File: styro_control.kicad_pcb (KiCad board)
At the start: 4 copper layers, 100.3 x 54 mm, 125 parts, among them J3 INPUT_PEDAL, J4 SWD, Q1 IRF7324, Q2 Q_NPN_BEC, Q3 Q_NMOS_GDS, Q4 Q_NPN_BEC, Q5 Q_NMOS_GDS, Q6 Q_NPN_BEC, Q7 Q_NMOS_GDS, Q8 Q_NPN_BEC, Q9 Q_NMOS_GDS, SW1 SW_RESET, SW2 switch_6_pin, SW3 SW_1, SW4 SW_2, SW5 SW_3, U1 STUSB4500QTR, U2 PAC1932-4, U3 ATSAMD21E18A-M, U4 INA226, U5 MC34063AD_copy, Y1 Crystal

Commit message: added footprints
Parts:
- added D10: +3.3V, LED_SMD:LED_0805_2012Metric_Pad1.15x1.40mm_HandSolder, F.Cu at (141.9, 53.0)
- added D11: TX_A6, LED_SMD:LED_0805_2012Metric_Pad1.15x1.40mm_HandSolder, F.Cu at (146.7, 53.0)
- added D8: VBUS, LED_SMD:LED_0805_2012Metric_Pad1.15x1.40mm_HandSolder, F.Cu at (141.9, 50.0)
- added D9: VSNK, LED_SMD:LED_0805_2012Metric_Pad1.15x1.40mm_HandSolder, F.Cu at (146.7, 50.0)
- added RN3: R_Pack04, Resistor_SMD:R_Array_Convex_4x0603, F.Cu at (141.6, 56.9)
- added SWD1: SWD, Connector_PinHeader_2.54mm:PinHeader_1x03_P2.54mm_Vertical, F.Cu at (133.9, 84.8)
- R2: value 100k -> 10K
- moved C18 0.78 mm to (134.1, 81.7), turned to 0 degrees
- moved R38 0.25 mm to (123.4, 81.7)
- moved C5 0.13 mm to (129.0, 81.7)
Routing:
- net unconnected-(USB_C1-PadB8): track 4.95 -> 0.00 mm
- net unconnected-(USB_C1-PadA8): track 0.00 -> 4.95 mm

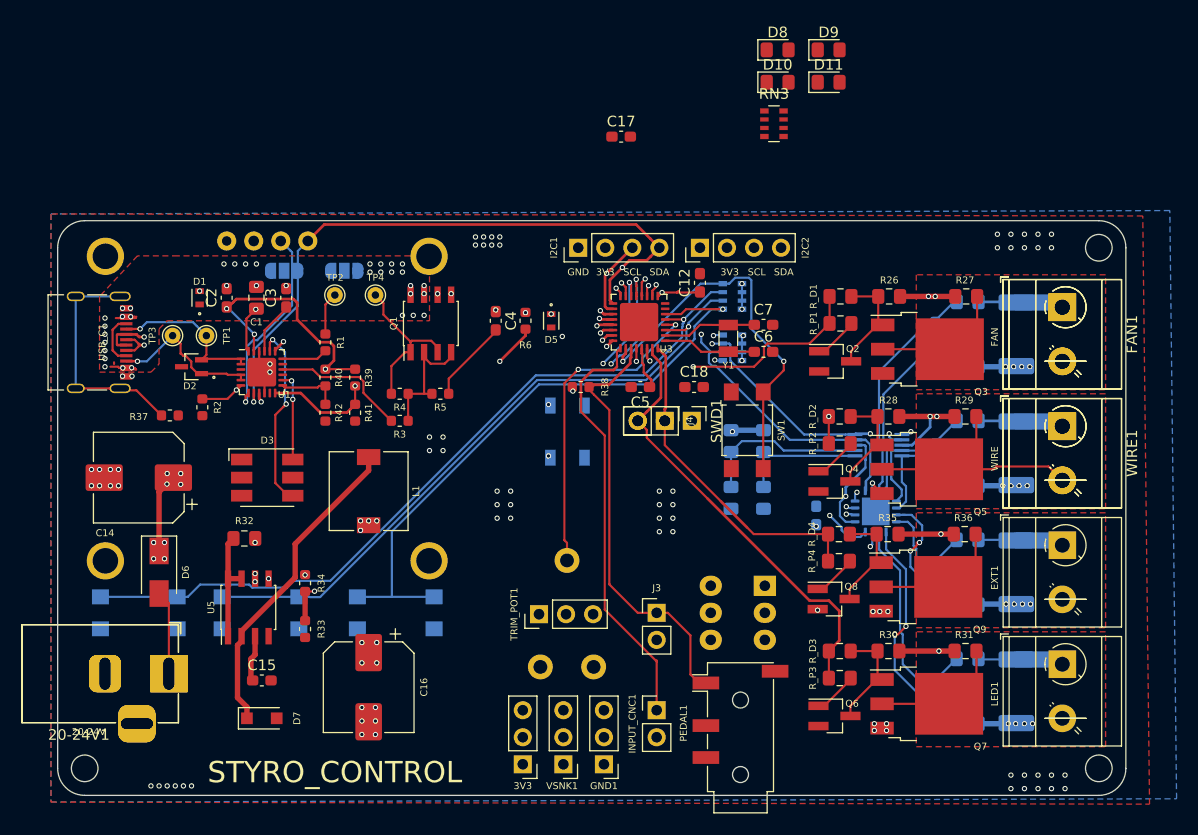
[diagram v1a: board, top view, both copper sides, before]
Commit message: added footprints
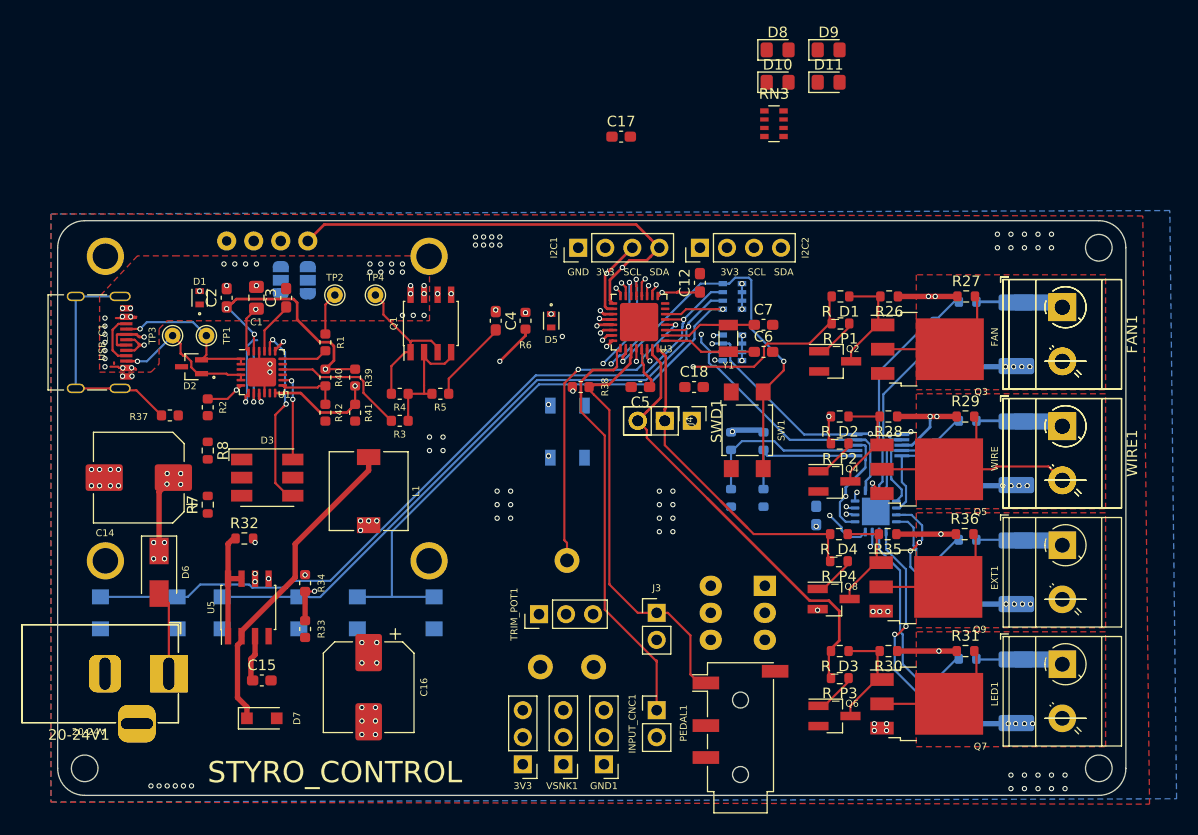
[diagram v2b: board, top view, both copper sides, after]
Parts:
- added R7: 1k, Resistor_SMD:R_0603_1608Metric, F.Cu at (88.4, 92.7)
- added R8: 1k, Resistor_SMD:R_0603_1608Metric, F.Cu at (88.4, 87.6)
- R11, R12, R13, R14, R15, R16, R17, R18, R26, R27, R28, R29, R30, R31, R32, R35, R36, R43, R44, R45, R46, R_D1, R_D2, R_D3, R_D4, R_P1, R_P2, R_P3, R_P4: footprint Resistor_SMD:R_0805_2012Metric_Pad1.15x1.40mm_HandSolder -> Resistor_SMD:R_0603_1608Metric
- moved JP2 3.54 mm to (97.8, 71.6), turned to -90 degrees
- moved JP1 0.94 mm to (95.2, 71.6), turned to -90 degrees
- moved R2 0.51 mm to (88.4, 83.6)
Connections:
- D3 pad 1: GND -> Net-(D3-Pad1)
- D3 pad 3: GND -> Net-(D3-Pad3)
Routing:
- net /SCL: track 199.7 -> 7.36 mm, vias 8 -> 1
- net /SDA: track 0.00 -> 168.9 mm, vias 0 -> 7
- net unconnected-(USB_C1-PadB8): track 0.00 -> 4.95 mm
- net unconnected-(USB_C1-PadA8): track 4.95 -> 0.00 mm
- net /RESET: track 50.1 -> 49.6 mm
- net GND: vias 89 -> 88

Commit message: added LEDs for VBUS,VSNK,3V3,TX
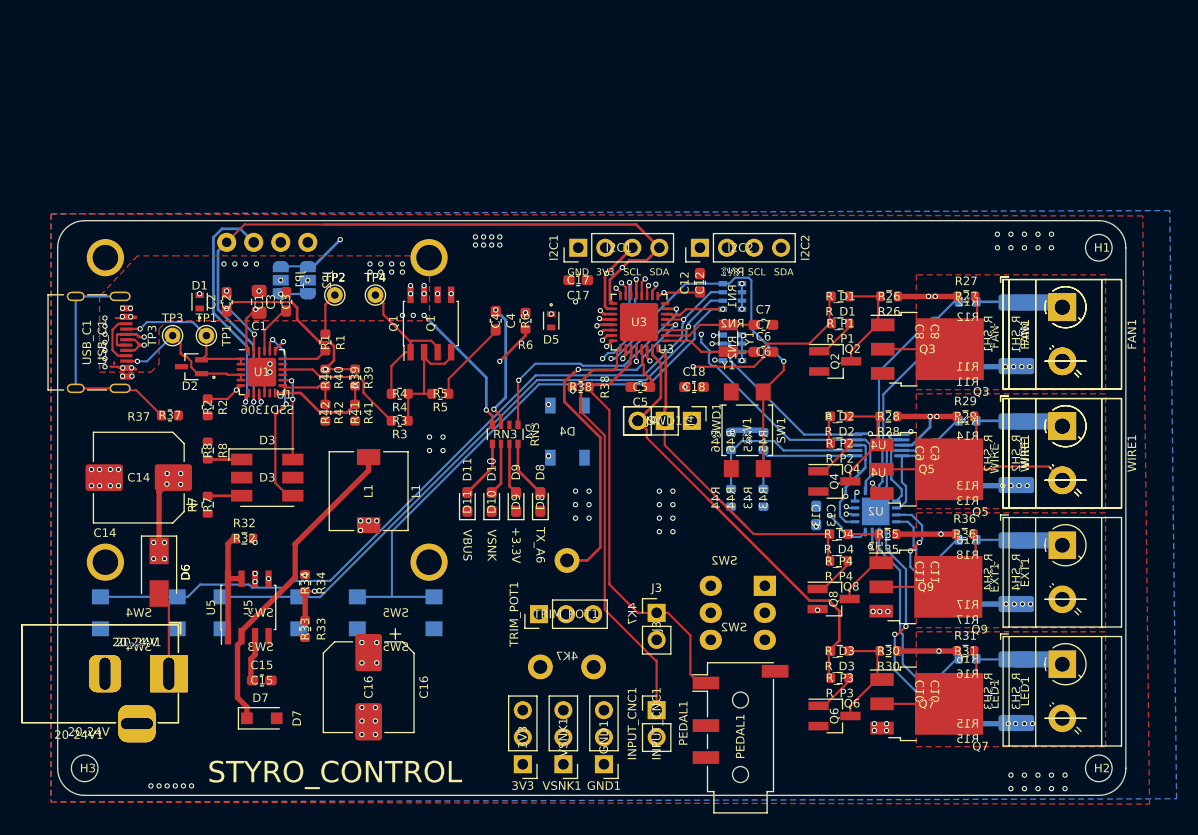
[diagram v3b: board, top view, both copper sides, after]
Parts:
- D10, D11, D8, D9: footprint LED_SMD:LED_0805_2012Metric_Pad1.15x1.40mm_HandSolder -> LED_SMD:LED_0603_1608Metric_Pad1.05x0.95mm_HandSolder
- moved D11 52.0 mm to (112.8, 92.5), turned to 90 degrees
- moved D9 51.6 mm to (117.3, 92.5), turned to 90 degrees
- moved D8 48.0 mm to (119.6, 92.5), turned to 90 degrees
- moved D10 47.7 mm to (115.1, 92.5), turned to 90 degrees
- moved RN3 38.6 mm to (116.3, 86.1), turned to -90 degrees
- moved C17 14.1 mm to (123.2, 71.6), turned to 180 degrees
- moved C1 0.46 mm to (93.2, 73.7)
- moved C2 0.38 mm to (90.2, 73.7)
- moved C3 0.38 mm to (95.8, 73.7)
- moved D1 0.38 mm to (87.6, 73.7)
- moved SSD1306 0.13 mm to (94.0, 83.3)
- turned JP1 to 90 degrees
- turned JP2 to 90 degrees
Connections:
- RN3 pad 1: /VBUS -> /TX_A6
- RN3 pad 2: /VSNK -> /+3.3V
- RN3 pad 3: /+3.3V -> /VSNK
- RN3 pad 4: /TX_A6 -> /VBUS
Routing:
- net /SCL: track 7.36 -> 109.9 mm, vias 1 -> 5
- net /SDA: track 168.9 -> 106.2 mm, vias 7 -> 3
- net /TX_A6: track 0.00 -> 23.3 mm, vias 0 -> 2
- net /VBUS: track 16.4 -> 29.4 mm, vias 30 -> 31
- net /VSNK: track 46.9 -> 58.8 mm, vias 38 -> 39
- net +3V3: track 16.2 -> 27.0 mm, vias 21 -> 23
- net Net-(D11-Pad2): track 0.00 -> 5.55 mm
- net Net-(D8-Pad2): track 0.00 -> 5.45 mm
- net Net-(D10-Pad2): track 0.00 -> 4.94 mm
- net Net-(D9-Pad2): track 0.00 -> 4.83 mm
- net /POT: track 36.1 -> 39.9 mm
- net Net-(JP2-Pad2): track 0.00 -> 3.56 mm, vias 0 -> 1
- net Net-(JP1-Pad2): track 0.00 -> 3.56 mm, vias 0 -> 1
- net Net-(D3-Pad3): track 0.00 -> 3.19 mm
- net Net-(D3-Pad1): track 0.00 -> 3.19 mm
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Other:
- board text added: "+3.3V"
- board text added: "TX_A6"
- board text added: "VBUS"
- board text added: "VSNK"
